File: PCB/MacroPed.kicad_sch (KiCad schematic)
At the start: 9 parts, among them J1 Conn_01x02_Socket, J2 Conn_01x02_Socket, J3 Conn_01x02_Socket, J4 Conn_01x02_Socket, J5 Conn_01x02_Socket, J6 Conn_01x02_Socket, J7 Conn_01x02_Socket, J8 Conn_01x02_Socket, U1 Pico

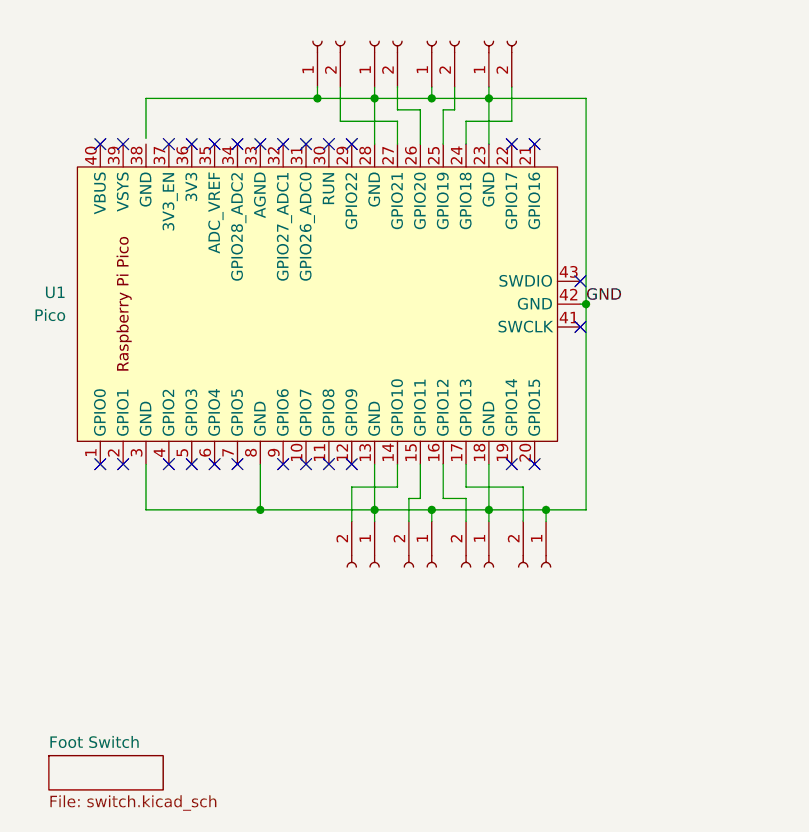
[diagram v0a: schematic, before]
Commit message: Separated daughterboard to sub-project, added mounting holes
Signed-off-by: Devnol <pgkoutsoumanis@gmail.com>
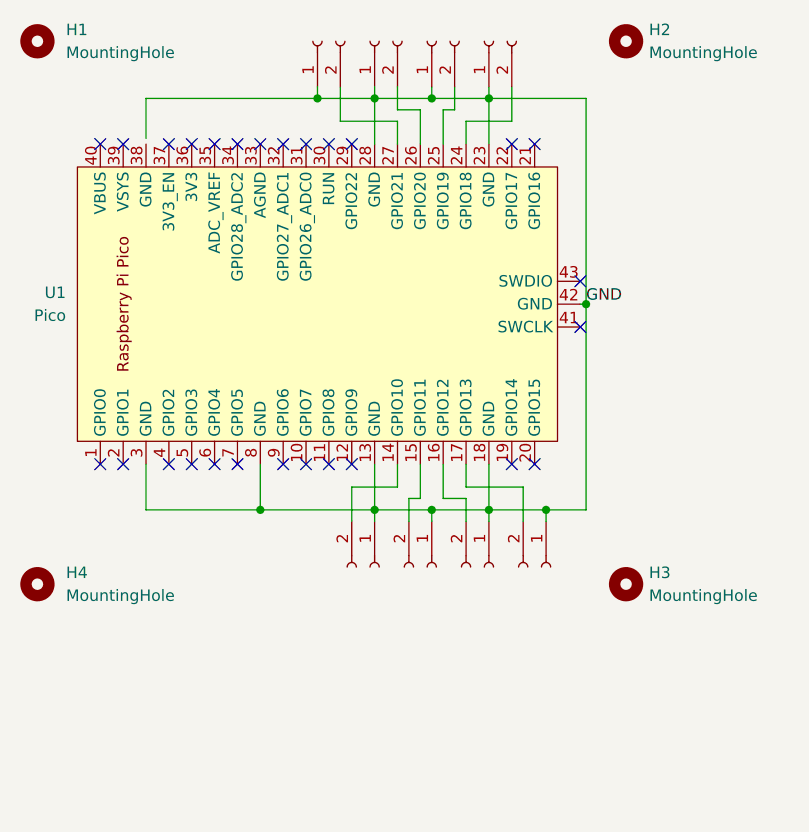
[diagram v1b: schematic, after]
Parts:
- added H1, H2, H3, H4: MountingHole, MountingHole:MountingHole_2.7mm_M2.5_DIN965, symbol Mechanical:MountingHole
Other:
- removed sheet Foot Switch
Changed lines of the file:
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@@
+    )
+  )
+  (symbol (lib_id "Mechanical:MountingHole") (at 29.845 84.455 0) (unit 1)
+    (in_bom yes) (on_board yes) (dnp no) (fields_autoplaced)
+    (property "Reference" "H4" (at 33.02 83.185 0)
+      (effects (font (size 1.27 1.27)) (justify left))
+    )
+    (property "Value" "MountingHole" (at 33.02 85.725 0)
+      (effects (font (size 1.27 1.27)) (justify left))
+    )
+    (property "Footprint" "MountingHole:MountingHole_2.7mm_M2.5_DIN965" (at 29.845 84.455 0)
+      (effects (font (size 1.27 1.27)) hide)
+    )
+    (property "Datasheet" "~" (at 29.845 84.455 0)
+      (effects (font (size 1.27 1.27)) hide)
+    )
+    (instances
+      (project "MacroPed"
+        (path "/13decee3-1b64-4c34-802a-57fdd4ff7914"
+          (reference "H4") (unit 1)
+        )
+      )
     )
   )
@@
         (path "/13decee3-1b64-4c34-802a-57fdd4ff7914"
           (reference "J4") (unit 1)
+        )
+      )
+    )
+  )
+  (symbol (lib_id "Mechanical:MountingHole") (at 95.25 24.13 0) (unit 1)
+    (in_bom yes) (on_board yes) (dnp no) (fields_autoplaced)
+    (property "Reference" "H2" (at 97.79 22.86 0)
+      (effects (font (size 1.27 1.27)) (justify left))
+    )
+    (property "Value" "MountingHole" (at 97.79 25.4 0)
+      (effects (font (size 1.27 1.27)) (justify left))
+    )
+    (property "Footprint" "MountingHole:MountingHole_2.7mm_M2.5_DIN965" (at 95.25 24.13 0)
+      (effects (font (size 1.27 1.27)) hide)
+    )
+    (property "Datasheet" "~" (at 95.25 24.13 0)
+      (effects (font (size 1.27 1.27)) hide)
+    )
+    (instances
+      (project "MacroPed"
+        (path "/13decee3-1b64-4c34-802a-57fdd4ff7914"
+          (reference "H2") (unit 1)
+        )
+      )
+    )
+  )
+  (symbol (lib_id "Mechanical:MountingHole") (at 29.845 24.13 0) (unit 1)
+    (in_bom yes) (on_board yes) (dnp no) (fields_autoplaced)
+    (property "Reference" "H1" (at 33.02 22.86 0)
+      (effects (font (size 1.27 1.27)) (justify left))
+    )
+    (property "Value" "MountingHole" (at 33.02 25.4 0)
+      (effects (font (size 1.27 1.27)) (justify left))
+    )
+    (property "Footprint" "MountingHole:MountingHole_2.7mm_M2.5_DIN965" (at 29.845 24.13 0)
+      (effects (font (size 1.27 1.27)) hide)
+    )
+    (property "Datasheet" "~" (at 29.845 24.13 0)
+      (effects (font (size 1.27 1.27)) hide)
+    )
+    (instances
+      (project "MacroPed"
+        (path "/13decee3-1b64-4c34-802a-57fdd4ff7914"
+          (reference "H1") (unit 1)
         )
       )
@@
     )
   )
+  (symbol (lib_id "Mechanical:MountingHole") (at 95.25 84.455 0) (unit 1)
+    (in_bom yes) (on_board yes) (dnp no) (fields_autoplaced)
+    (property "Reference" "H3" (at 97.79 83.185 0)
+      (effects (font (size 1.27 1.27)) (justify left))
+    )
+    (property "Value" "MountingHole" (at 97.79 85.725 0)
+      (effects (font (size 1.27 1.27)) (justify left))
+    )
+    (property "Footprint" "MountingHole:MountingHole_2.7mm_M2.5_DIN965" (at 95.25 84.455 0)
+      (effects (font (size 1.27 1.27)) hide)
+    )
+    (property "Datasheet" "~" (at 95.25 84.455 0)
+      (effects (font (size 1.27 1.27)) hide)
+    )
+    (instances
+      (project "MacroPed"
+        (path "/13decee3-1b64-4c34-802a-57fdd4ff7914"
+          (reference "H3") (unit 1)
+        )
+      )
+    )
+  )
   (symbol (lib_id "Connector:Conn_01x02_Socket") (at 73.66 24.13 90) (unit 1)
     (in_bom yes) (on_board yes) (dnp no)
@@
       )
     )
-  )
-  (sheet (at 31.115 103.505) (size 12.7 3.81) (fields_autoplaced)
-    (stroke (width 0.1524) (type solid))
-    (fill (color 0 0 0 0.0000))
-    (property "Sheetname" "Foot Switch" (at 31.115 102.7934 0)
-      (effects (font (size 1.27 1.27)) (justify left bottom))
-    )
-    (property "Sheetfile" "switch.kicad_sch" (at 31.115 107.8996 0)
-      (effects (font (size 1.27 1.27)) (justify left top))
-    )
-    (instances
-      (project "MacroPed"
-        (path "/13decee3-1b64-4c34-802a-57fdd4ff7914" (page "2"))
-      )
-    )

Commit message: Move connectors to one side, change dimensions to proper units
Signed-off-by: Devnol <pgkoutsoumanis@gmail.com>
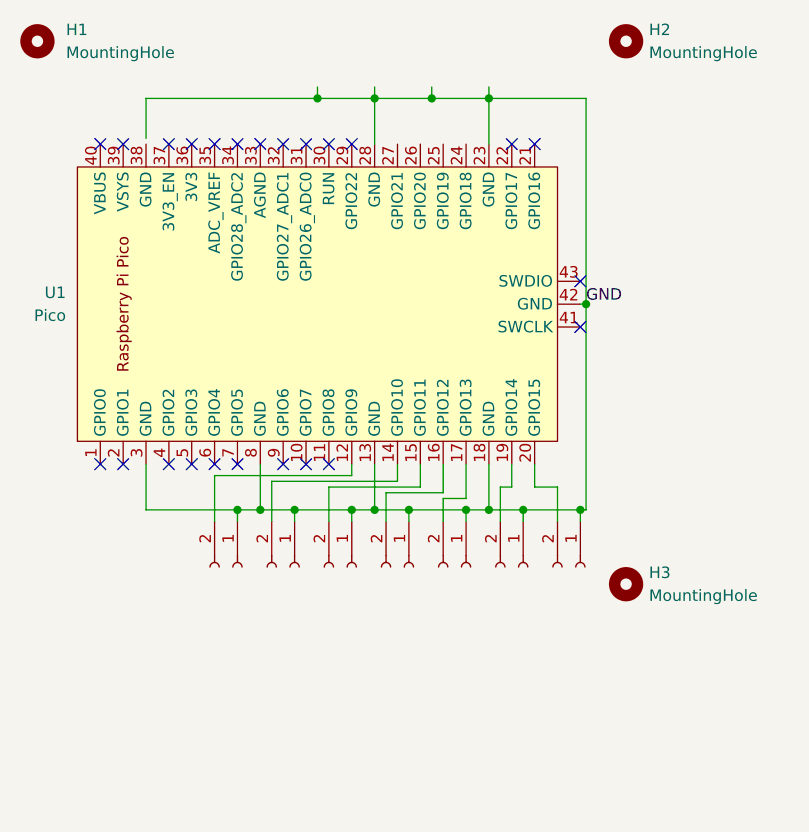
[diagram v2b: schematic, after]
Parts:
- removed H4: MountingHole, MountingHole:MountingHole_2.7mm_M2.5_DIN965, symbol Mechanical:MountingHole
- removed J7: Conn_01x02_Socket, Connector_JST:JST_PH_S2B-PH-K_1x02_P2.00mm_Horizontal, symbol Connector:Conn_01x02_Socket
- renumbered J5 to J1, J6 to J2, J8 to J3, J1 to J4, J2 to J5, J3 to J6, J4 to J7
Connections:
- net at J6.2 (Pin_2): now also U1.19 (GPIO14); no longer U1.16 (GPIO12)
- net at J7.2 (Pin_2): now also U1.20 (GPIO15); no longer U1.17 (GPIO13)
- net at U1.12 (GPIO9): now also J1.2 (Pin_2)
- net at U1.14 (GPIO10): now also J2.2 (Pin_2); no longer J4.2 (Pin_2)
- net at U1.15 (GPIO11): now also J3.2 (Pin_2); no longer J5.2 (Pin_2)
- net at U1.24 (GPIO18): no longer J1.2 (Pin_2)
- net at U1.25 (GPIO19): no longer J2.2 (Pin_2)
- net at U1.27 (GPIO21): no longer J3.2 (Pin_2)
- new net: J4.2 (Pin_2), U1.16 (GPIO12)
- new net: J5.2 (Pin_2), U1.17 (GPIO13)
- no-connect marks 27 -> 24

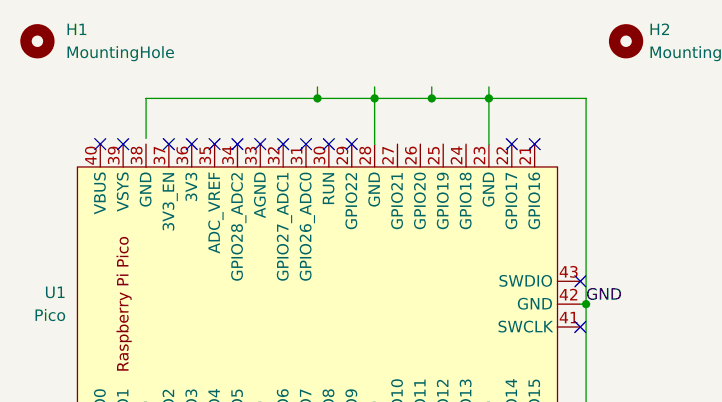
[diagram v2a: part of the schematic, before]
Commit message: Moved JST connector to edge of footboard
Signed-off-by: Devnol <pgkoutsoumanis@gmail.com>
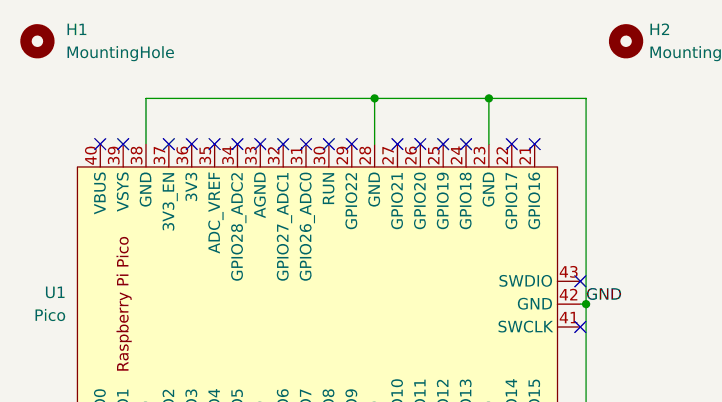
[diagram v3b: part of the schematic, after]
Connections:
- net GND: now also U1.38 (GND)
- no-connect marks 24 -> 28
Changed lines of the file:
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@@
   (junction (at 54.61 76.2) (diameter 0) (color 0 0 0 0)
   )
-  (junction (at 67.31 30.48) (diameter 0) (color 0 0 0 0)
-  )
-  (junction (at 60.96 30.48) (diameter 0) (color 0 0 0 0)
-  )
   (junction (at 90.17 76.2) (diameter 0) (color 0 0 0 0)
-  )
-  (junction (at 73.66 30.48) (diameter 0) (color 0 0 0 0)
   )
   (junction (at 77.47 76.2) (diameter 0) (color 0 0 0 0)
@@
   (junction (at 90.805 53.34) (diameter 0) (color 0 0 0 0)
   )
+  (junction (at 67.31 30.48) (diameter 0) (color 0 0 0 0)
+  )
   (no_connect (at 90.17 50.8))
+  (no_connect (at 74.93 35.56))
   (no_connect (at 59.69 71.12))
   (no_connect (at 39.37 71.12))
   (no_connect (at 52.07 71.12))
   (no_connect (at 57.15 35.56))
+  (no_connect (at 69.85 35.56))
   (no_connect (at 62.23 35.56))
   (no_connect (at 59.69 35.56))
@@
   (no_connect (at 44.45 35.56))
   (no_connect (at 62.23 71.12))
+  (no_connect (at 77.47 35.56))
   (no_connect (at 52.07 35.56))
   (no_connect (at 64.77 35.56))
+  (no_connect (at 72.39 35.56))
   (no_connect (at 36.83 35.56))
   (no_connect (at 90.17 55.88))
@@
     (stroke (width 0) (type default))
   )
-  (wire (pts (xy 67.31 30.48) (xy 60.96 30.48))
-    (stroke (width 0) (type default))
-  )
   (wire (pts (xy 81.28 77.47) (xy 81.28 73.66))
     (stroke (width 0) (type default))
   )
   (wire (pts (xy 69.85 73.025) (xy 69.85 71.12))
+    (stroke (width 0) (type default))
+  )
+  (wire (pts (xy 41.91 30.48) (xy 41.91 35.56))
     (stroke (width 0) (type default))
   )
@@
     (stroke (width 0) (type default))
   )
-  (wire (pts (xy 60.96 30.48) (xy 60.96 29.21))
-    (stroke (width 0) (type default))
-  )
   (wire (pts (xy 68.58 74.295) (xy 74.93 74.295))
     (stroke (width 0) (type default))
   )
   (wire (pts (xy 85.09 73.66) (xy 85.09 71.12))
-    (stroke (width 0) (type default))
-  )
-  (wire (pts (xy 41.91 30.48) (xy 60.96 30.48))
     (stroke (width 0) (type default))
   )
@@
   )
   (wire (pts (xy 64.77 76.2) (xy 64.77 77.47))
-    (stroke (width 0) (type default))
-  )
-  (wire (pts (xy 80.01 29.21) (xy 80.01 30.48))
     (stroke (width 0) (type default))
   )
@@
     (stroke (width 0) (type default))
   )
-  (wire (pts (xy 73.66 30.48) (xy 67.31 30.48))
+  (wire (pts (xy 67.31 30.48) (xy 80.01 30.48))
     (stroke (width 0) (type default))
   )
   (wire (pts (xy 55.88 77.47) (xy 55.88 73.025))
-    (stroke (width 0) (type default))
-  )
-  (wire (pts (xy 73.66 30.48) (xy 80.01 30.48))
     (stroke (width 0) (type default))
   )
@@
     (stroke (width 0) (type default))
   )
+  (wire (pts (xy 67.31 30.48) (xy 41.91 30.48))
+    (stroke (width 0) (type default))
+  )
   (wire (pts (xy 41.91 71.12) (xy 41.91 76.2))
     (stroke (width 0) (type default))
@@
     (stroke (width 0) (type default))
   )
-  (wire (pts (xy 67.31 30.48) (xy 67.31 29.21))
-    (stroke (width 0) (type default))
-  )
-  (wire (pts (xy 73.66 30.48) (xy 73.66 29.21))
-    (stroke (width 0) (type default))
-  )
   (wire (pts (xy 83.82 76.2) (xy 90.17 76.2))
     (stroke (width 0) (type default))
@@
     (stroke (width 0) (type default))
   )
-  (wire (pts (xy 41.91 34.925) (xy 41.91 30.48))
-    (stroke (width 0) (type default))
-  )
